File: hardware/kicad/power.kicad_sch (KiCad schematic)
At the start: 18 parts, among them Q2 PMV32UP, Q7 DMG1012UW, U10 RT9080-33GJ5, U10 TPS7A0328DBVR, U12 TPS7A0333DBVR, U3 TPS22917DBVR

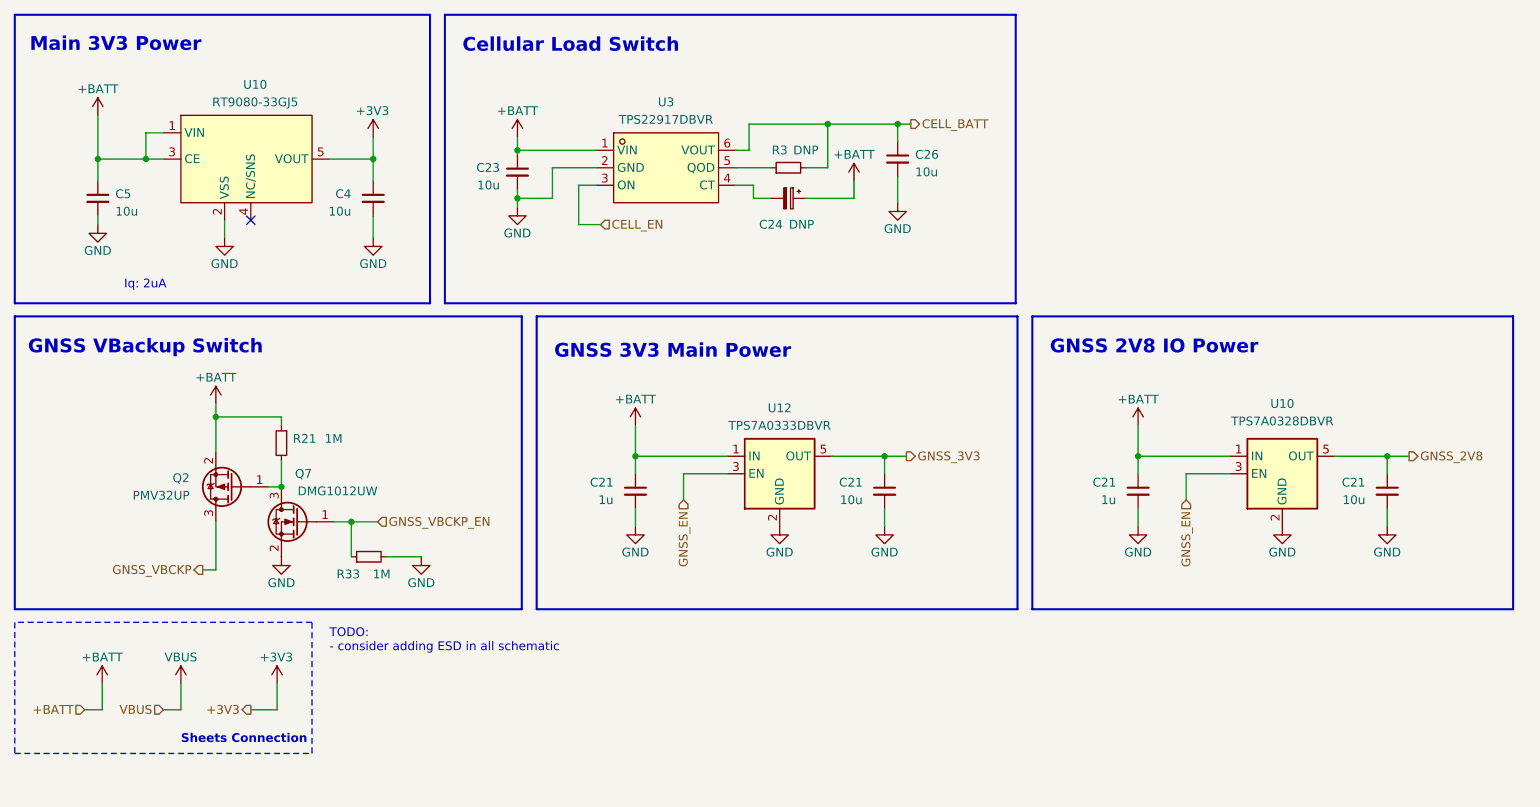
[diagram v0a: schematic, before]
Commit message: update to KiCAD 8 and add cell power regulator
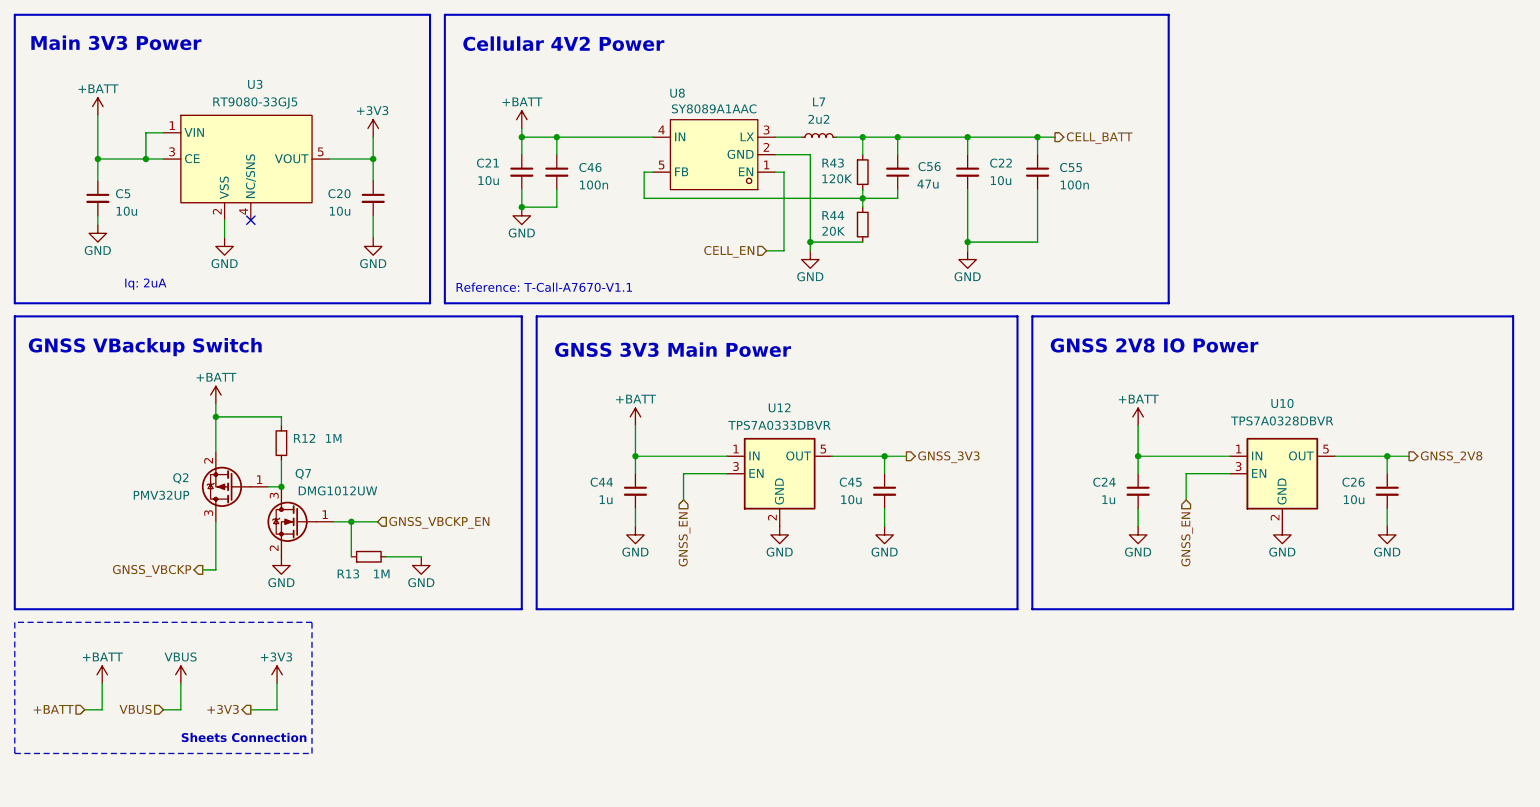
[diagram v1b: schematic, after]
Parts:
- removed C23, C26: 10u, Capacitor_SMD:C_0603_1608Metric, symbol Device:C_Small
- removed C24: DNP, Capacitor_Tantalum_SMD:CP_EIA-3528-15_AVX-H, symbol Device:C_Polarized_Small
- removed R3: DNP, Resistor_SMD:R_0603_1608Metric, symbol Device:R_Small
- removed U3: TPS22917DBVR, Package_TO_SOT_SMD:SOT-23-6, symbol bwlc1a:TPS22917DBVR
- added C21, C22: 10u, Capacitor_SMD:C_0603_1608Metric, symbol Device:C_Small
- added C46, C55: 100n, Capacitor_SMD:C_0603_1608Metric, symbol Device:C_Small
- added C56: 47u, Capacitor_SMD:C_0603_1608Metric, symbol Device:C_Small
- added L7: 2u2, bwlc1a:IND-SMD_L3.0-W3.0_LVS303015H-2R2M-N, symbol Device:L_Small
- added R43: 120K, Resistor_SMD:R_0603_1608Metric, symbol Device:R_Small
- added R44: 20K, Resistor_SMD:R_0603_1608Metric, symbol Device:R_Small
- added U8: SY8089A1AAC, Package_TO_SOT_SMD:SOT-23-5, symbol bwlc1a:SY8089A1AAC
- renumbered C4 to C20, C21 to C24, C21 to C26, C21 to C44, C21 to C45, R21 to R12, R33 to R13, U10 to U3
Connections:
- net +BATT: now also C21.1, C46.1, U8.4 (IN)
- net CELL_BATT: now also C22.1, C55.1, C56.2, L7.2, R43.1
- net CELL_EN: now also U8.1 (EN)
- net GND: now also C21.2, C22.2, C46.2, C55.2, R44.2, U8.2 (GND)
- new net: C56.1, R43.2, R44.1, U8.5 (FB)
- new net: L7.1, U8.3 (LX)
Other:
- note added: "Cellular 4V2 Power"
- note added: "Reference: T-Call-A7670-V1.1"
- note removed: "Cellular Load Switch"
- note removed: "TODO: - consider adding ESD in all schematic"

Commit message: GNSS power uses cheaper LDO
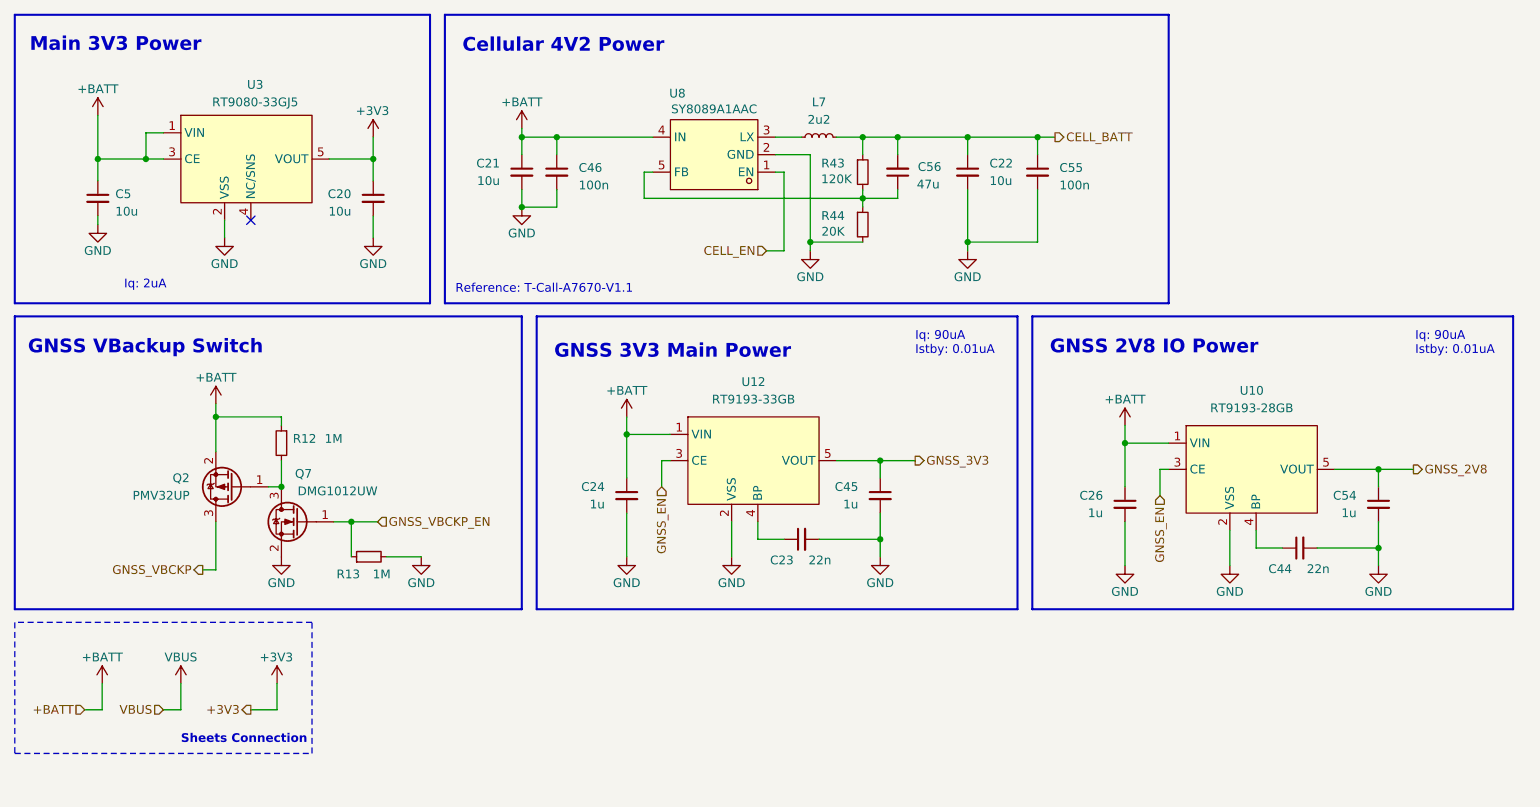
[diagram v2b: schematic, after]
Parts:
- removed U10: TPS7A0328DBVR, Package_TO_SOT_SMD:SOT-23-5, symbol Regulator_Linear:TPS7A0508PDBV
- removed U12: TPS7A0333DBVR, Package_TO_SOT_SMD:SOT-23-5, symbol Regulator_Linear:TPS7A0508PDBV
- added C23: 22n, Capacitor_SMD:C_0402_1005Metric, symbol Device:C_Small
- added C54: 1u, Capacitor_SMD:C_0402_1005Metric, symbol Device:C_Small
- added U10: RT9193-28GB, Package_TO_SOT_SMD:SOT-23-5, symbol bwlc1a:RT9193
- added U12: RT9193-33GB, Package_TO_SOT_SMD:SOT-23-5, symbol bwlc1a:RT9193
- C24: footprint Capacitor_SMD:C_0603_1608Metric -> Capacitor_SMD:C_0402_1005Metric; Distributor Link https://www.lcsc.com/product-detail/Multilayer-Ceramic-Capacitors-MLCC-SMD-SMT_Samsung-Electro-Mechanics-CL10A106KP8NNNC_C19702.html -> https://www.lcsc.com/product-detail/Multilayer-Ceramic-Capacitors-MLCC-SMD-SMT_Murata-Electronics-GRM155Z71A105KE01D_C528974.html; Distributor Part Number C19702 -> C528974; Id 1 -> (none); Manufacture Samsung Electro-Mechanics -> (none); Manufacture Part Number CL10A106KP8NNNC -> (none); Manufacturer (none) -> Murata Electronics; Manufacturer Part Number (none) -> GRM155Z71A105KE01D; Type SMD -> (none)
- C26, C45: value 10u -> 1u; footprint Capacitor_SMD:C_0603_1608Metric -> Capacitor_SMD:C_0402_1005Metric; Distributor Link https://www.lcsc.com/product-detail/Multilayer-Ceramic-Capacitors-MLCC-SMD-SMT_Samsung-Electro-Mechanics-CL10A106KP8NNNC_C19702.html -> https://www.lcsc.com/product-detail/Multilayer-Ceramic-Capacitors-MLCC-SMD-SMT_Murata-Electronics-GRM155Z71A105KE01D_C528974.html; Distributor Part Number C19702 -> C528974; Id 1 -> (none); Manufacture Samsung Electro-Mechanics -> (none); Manufacture Part Number CL10A106KP8NNNC -> (none); Manufacturer (none) -> Murata Electronics; Manufacturer Part Number (none) -> GRM155Z71A105KE01D; Type SMD -> (none)
- C44: value 1u -> 22n; footprint Capacitor_SMD:C_0603_1608Metric -> Capacitor_SMD:C_0402_1005Metric; Distributor Link https://www.lcsc.com/product-detail/Multilayer-Ceramic-Capacitors-MLCC-SMD-SMT_Samsung-Electro-Mechanics-CL10A106KP8NNNC_C19702.html -> https://www.lcsc.com/product-detail/Multilayer-Ceramic-Capacitors-MLCC-SMD-SMT_YAGEO-CC0402KRX7R9BB223_C107026.html; Distributor Part Number C19702 -> C107026; Id 1 -> (none); Manufacture Samsung Electro-Mechanics -> (none); Manufacture Part Number CL10A106KP8NNNC -> (none); Manufacturer (none) -> YAGEO; Manufacturer Part Number (none) -> CC0402KRX7R9BB223; Type SMD -> (none)
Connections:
- net +BATT: now also C26.1, U10.1 (VIN), U12.1 (VIN); no longer C44.1
- net GND: now also C23.2, C54.2, U10.2 (VSS), U12.2 (VSS)
- net GNSS_2V8: now also C54.1, U10.5 (VOUT); no longer C26.1
- net GNSS_3V3: now also U12.5 (VOUT)
- net GNSS_EN: now also U10.3 (CE), U12.3 (CE)
- new net: C44.1, U10.4 (BP)
- new net: C23.1, U12.4 (BP)
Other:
- note added: "Iq: 90uA Istby: 0.01uA"
- moved on the sheet: C45

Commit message: Revert "GNSS power uses cheaper LDO"
This reverts commit 0e9862c17de09eba40dda24cbaa62e3753723199.
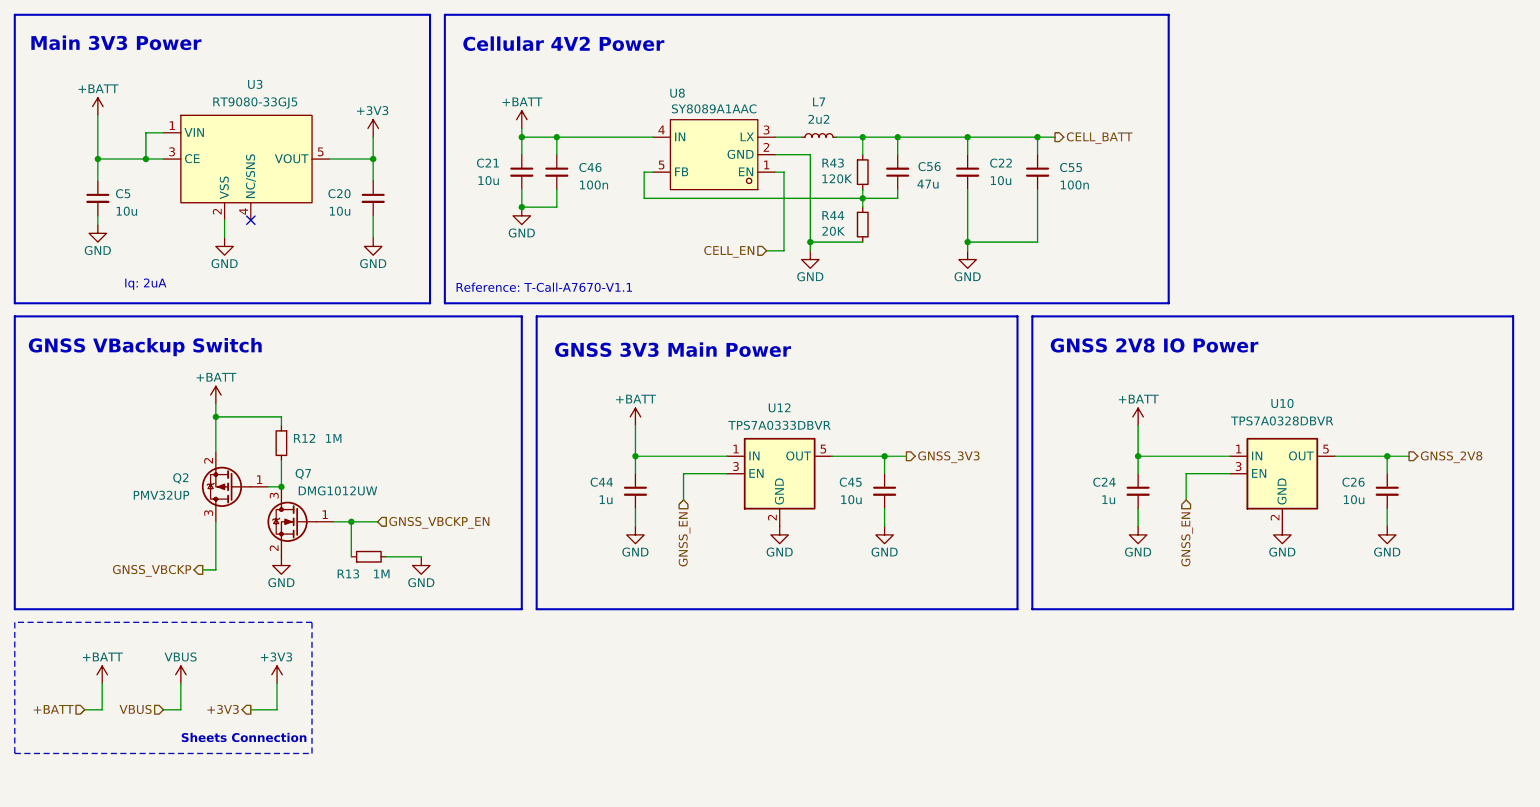
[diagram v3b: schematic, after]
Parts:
- removed C23: 22n, Capacitor_SMD:C_0402_1005Metric, symbol Device:C_Small
- removed C54: 1u, Capacitor_SMD:C_0402_1005Metric, symbol Device:C_Small
- removed U10: RT9193-28GB, Package_TO_SOT_SMD:SOT-23-5, symbol bwlc1a:RT9193
- removed U12: RT9193-33GB, Package_TO_SOT_SMD:SOT-23-5, symbol bwlc1a:RT9193
- added U10: TPS7A0328DBVR, Package_TO_SOT_SMD:SOT-23-5, symbol Regulator_Linear:TPS7A0508PDBV
- added U12: TPS7A0333DBVR, Package_TO_SOT_SMD:SOT-23-5, symbol Regulator_Linear:TPS7A0508PDBV
- C24: footprint Capacitor_SMD:C_0402_1005Metric -> Capacitor_SMD:C_0603_1608Metric; Distributor Link https://www.lcsc.com/product-detail/Multilayer-Ceramic-Capacitors-MLCC-SMD-SMT_Murata-Electronics-GRM155Z71A105KE01D_C528974.html -> https://www.lcsc.com/product-detail/Multilayer-Ceramic-Capacitors-MLCC-SMD-SMT_Samsung-Electro-Mechanics-CL10A106KP8NNNC_C19702.html; Distributor Part Number C528974 -> C19702; Id (none) -> 1; Manufacture (none) -> Samsung Electro-Mechanics; Manufacture Part Number (none) -> CL10A106KP8NNNC; Manufacturer Murata Electronics -> (none); Manufacturer Part Number GRM155Z71A105KE01D -> (none); Type (none) -> SMD
- C26, C45: value 1u -> 10u; footprint Capacitor_SMD:C_0402_1005Metric -> Capacitor_SMD:C_0603_1608Metric; Distributor Link https://www.lcsc.com/product-detail/Multilayer-Ceramic-Capacitors-MLCC-SMD-SMT_Murata-Electronics-GRM155Z71A105KE01D_C528974.html -> https://www.lcsc.com/product-detail/Multilayer-Ceramic-Capacitors-MLCC-SMD-SMT_Samsung-Electro-Mechanics-CL10A106KP8NNNC_C19702.html; Distributor Part Number C528974 -> C19702; Id (none) -> 1; Manufacture (none) -> Samsung Electro-Mechanics; Manufacture Part Number (none) -> CL10A106KP8NNNC; Manufacturer Murata Electronics -> (none); Manufacturer Part Number GRM155Z71A105KE01D -> (none); Type (none) -> SMD
- C44: value 22n -> 1u; footprint Capacitor_SMD:C_0402_1005Metric -> Capacitor_SMD:C_0603_1608Metric; Distributor Link https://www.lcsc.com/product-detail/Multilayer-Ceramic-Capacitors-MLCC-SMD-SMT_YAGEO-CC0402KRX7R9BB223_C107026.html -> https://www.lcsc.com/product-detail/Multilayer-Ceramic-Capacitors-MLCC-SMD-SMT_Samsung-Electro-Mechanics-CL10A106KP8NNNC_C19702.html; Distributor Part Number C107026 -> C19702; Id (none) -> 1; Manufacture (none) -> Samsung Electro-Mechanics; Manufacture Part Number (none) -> CL10A106KP8NNNC; Manufacturer YAGEO -> (none); Manufacturer Part Number CC0402KRX7R9BB223 -> (none); Type (none) -> SMD
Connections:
- net +BATT: now also C44.1, U10.1 (IN), U12.1 (IN); no longer C26.1
- net GND: now also U10.2 (GND), U12.2 (GND)
- net GNSS_2V8: now also C26.1, U10.5 (OUT)
- net GNSS_3V3: now also U12.5 (OUT)
- net GNSS_EN: now also U10.3 (EN), U12.3 (EN)
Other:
- note removed: "Iq: 90uA Istby: 0.01uA"
- moved on the sheet: C45

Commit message: update bill of materials
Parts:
- C20, C21, C22, C5: Id 1 -> (none); Manufacture Samsung Electro-Mechanics -> (none); Manufacture Part Number CL10A106KP8NNNC -> (none); Manufacturer (none) -> Samsung Electro-Mechanics; Manufacturer Part Number (none) -> CL10A106KP8NNNC; Type SMD -> (none)
- C24, C44: Distributor Link https://www.lcsc.com/product-detail/Multilayer-Ceramic-Capacitors-MLCC-SMD-SMT_Samsung-Electro-Mechanics-CL10A106KP8NNNC_C19702.html -> https://www.lcsc.com/product-detail/Multilayer-Ceramic-Capacitors-MLCC-SMD-SMT_Samsung-Electro-Mechanics-CL10B105KO8NNNC_C59782.html; Distributor Part Number C19702 -> C59782; Id 1 -> (none); Manufacture Samsung Electro-Mechanics -> (none); Manufacture Part Number CL10A106KP8NNNC -> (none); Manufacturer (none) -> Samsung Electro-Mechanics; Manufacturer Part Number (none) -> CL10B105KO8NNNC; Type SMD -> (none)
- C26, C45: value 10u -> 1u; Distributor Link https://www.lcsc.com/product-detail/Multilayer-Ceramic-Capacitors-MLCC-SMD-SMT_Samsung-Electro-Mechanics-CL10A106KP8NNNC_C19702.html -> https://www.lcsc.com/product-detail/Multilayer-Ceramic-Capacitors-MLCC-SMD-SMT_Samsung-Electro-Mechanics-CL10B105KO8NNNC_C59782.html; Distributor Part Number C19702 -> C59782; Id 1 -> (none); Manufacture Samsung Electro-Mechanics -> (none); Manufacture Part Number CL10A106KP8NNNC -> (none); Manufacturer (none) -> Samsung Electro-Mechanics; Manufacturer Part Number (none) -> CL10B105KO8NNNC; Type SMD -> (none)
- C46, C55: Distributor (none) -> LCSC; Distributor Link (none) -> https://www.lcsc.com/product-detail/Multilayer-Ceramic-Capa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; Distributor Part Number (none) -> C66501; Manufacturer (none) -> Samsung Electro-Mechanics; Manufacturer Part Number (none) -> CL10B104KO8NNNC
- C56: Distributor (none) -> LCSC; Distributor Link (none) -> https://www.lcsc.com/product-detail/Multilayer-Ceramic-Capa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; Distributor Part Number (none) -> C140782; Manufacturer (none) -> Murata Electronics; Manufacturer Part Number (none) -> GRM188R60J476ME15D
- L7: Distributor (none) -> LCSC; Distributor Link (none) -> https://www.lcsc.com/product-detail/Power-Inductors_Chilisi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; Distributor Part Number (none) -> C285837; Manufacturer (none) -> Chilisin Elec; Manufacturer Part Number (none) -> LVS303015-2R2M-N
- Q2: Distributor (none) -> LCSC; Distributor Link (none) -> https://www.lcsc.com/product-detail/MOSFETs_TECH-PUBLIC-PMV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; Distributor Part Number (none) -> C2959851; Manufacturer (none) -> TECH PUBLIC; Manufacturer Part Number (none) -> PMV32UP
- Q7: Distributor (none) -> LCSC; Distributor Link (none) -> https://www.lcsc.com/product-detail/MOSFETs_Diodes-Incorpor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; Distributor Part Number (none) -> C156390; Manufacturer (none) -> Diodes Incorporated; Manufacturer Part Number (none) -> DMG1012UW-7
- R12, R13: Distributor (none) -> LCSC; Distributor Link (none) -> https://www.lcsc.com/product-detail/Chip-Resistor-Surface-M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; Distributor Part Number (none) -> C22935; Manufacturer (none) -> UNI-ROYAL(Uniroyal Elec); Manufacturer Part Number (none) -> 0603WAF1004T5E
- R43: Distributor (none) -> LCSC; Distributor Link (none) -> https://www.lcsc.com/product-detail/Chip-Resistor-Surface-M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; Distributor Part Number (none) -> C25808; Manufacturer (none) -> UNI-ROYAL(Uniroyal Elec); Manufacturer Part Number (none) -> 0603WAF1203T5E
- R44: Distributor (none) -> LCSC; Distributor Link (none) -> https://www.lcsc.com/product-detail/Chip-Resistor-Surface-M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; Distributor Part Number (none) -> C4184; Manufacturer (none) -> UNI-ROYAL(Uniroyal Elec); Manufacturer Part Number (none) -> 0603WAF2002T5E
- U10: Distributor (none) -> LCSC; Distributor Link (none) -> https://www.lcsc.com/product-detail/Linear-Voltage-Regulato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; Distributor Part Number (none) -> C2862669; Manufacturer (none) -> Texas Instruments; Manufacturer Part Number (none) -> TPS7A0328DBVR
- U12: Distributor (none) -> LCSC; Distributor Link (none) -> https://www.lcsc.com/product-detail/Linear-Voltage-Regulato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; Distributor Part Number (none) -> C2873330; Manufacturer (none) -> Texas Instruments; Manufacturer Part Number (none) -> TPS7A0333DBVR
- U3: Part Description Linear Voltage Regulators 75dB@(1kHz) 600mA 3.3V -> (none)
- U8: Distributor (none) -> LCSC; Distributor Link (none) -> https://www.lcsc.com/product-detail/New-Quadratic-Unclassif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; Distributor Part Number (none) -> C479074; Manufacturer (none) -> Silergy Corp; Manufacturer Part Number (none) -> SY8089A1AAC

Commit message: update bill of materials
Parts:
- R43: value 120K -> 120k
- R44: value 20K -> 20k
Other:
- note added: "- high PSRR LDO is preferred"
- note added: "- switching DC-DC power supply is NOT recommended"
- note added: "Iq: 200nA"
- note added: "note:"
- moved on the sheet: C24, C26, C44, C45, Q2, Q7, R12, R13, U10, U12

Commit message: add page info
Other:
- company: (none) -> Teapot Laboratories
- title: (none) -> Power
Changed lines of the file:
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@@
 	(generator_version "8.0")
 	(paper "A4")
+	(title_block
+		(title "Power")
+		(date "2024-05-17")
+		(rev "1")
+		(company "Teapot Laboratories")
+	)
 	(junction
 		(at 60.96 56.515)
